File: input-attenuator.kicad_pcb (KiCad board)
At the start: 2 copper layers, 90.2 x 55.8 mm, 100 parts, among them J1 DC_INTF, J2 DC_INTF, J3 RX, J4 ANT, J5 TX, K1 EE2-5TNU-L, K2 EE2-5TNU-L, K3 EE2-5TNU-L, K4 EE2-5TNU-L, Q1 BC858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

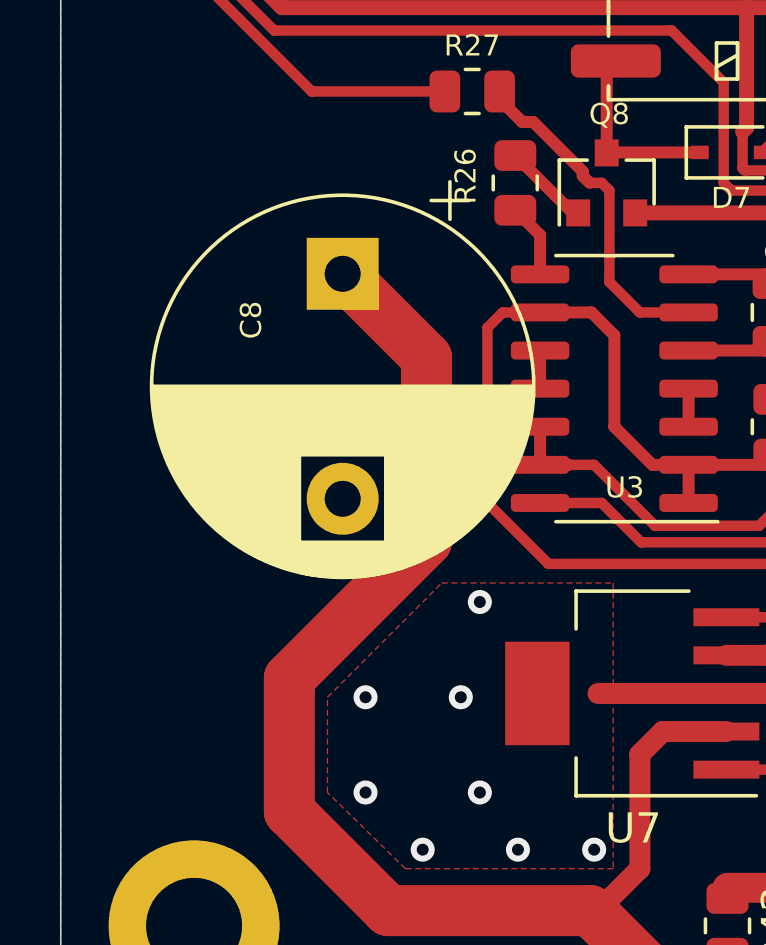
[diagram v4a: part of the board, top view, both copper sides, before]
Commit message: Layout: rotated C8
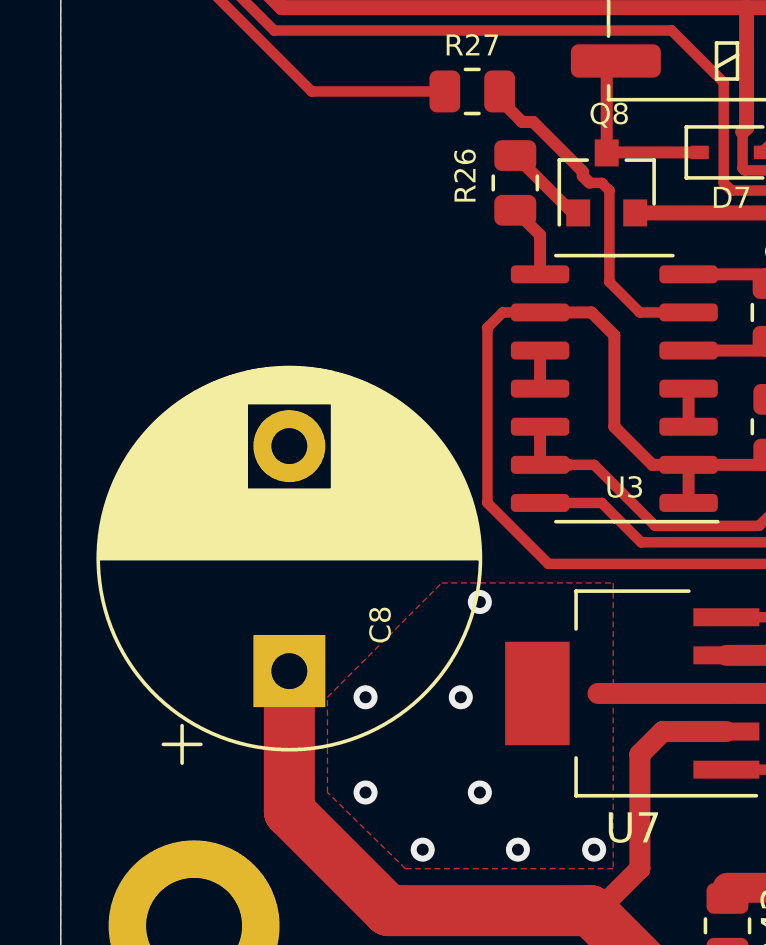
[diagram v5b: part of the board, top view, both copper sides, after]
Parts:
- moved C8 13.4 mm to (71.1, 68.3), turned to 90 degrees
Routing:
- net /Vin2: track 140.4 -> 123.9 mm
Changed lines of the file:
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@@
   )
   (footprint "Capacitor_THT:CP_Radial_D12.5mm_P7.50mm" (layer "F.Cu")
-    (at 72.898 55.100041 -90)
+    (at 71.12 68.343959 90)
     (descr "CP, Radial series, Radial, pin pitch=7.50mm, , diameter=12.5mm, Electrolytic Capacitor")
     (tags "CP Radial series Radial pin pitch 7.50mm  diameter 12.5mm Electrolytic Capacitor")
@@
     (fp_line (start -1.616489 -2.7375) (end -0.366489 -2.7375) (layer "F.Fab") (width 0.1))
     (fp_circle (center 3.75 0) (end 10 0) (layer "F.Fab") (width 0.1) (fill none))
-    (pad "1" thru_hole rect (at 0 0 270) (locked) (size 2.4 2.4) (drill 1.2) (layers *.Cu *.Mask)
+    (pad "1" thru_hole rect (at 0 0 90) (locked) (size 2.4 2.4) (drill 1.2) (layers *.Cu *.Mask)
       (net 4 "/Vin2") (pintype "passive"))
-    (pad "2" thru_hole circle (at 7.5 0 270) (locked) (size 2.4 2.4) (drill 1.2) (layers *.Cu *.Mask)
+    (pad "2" thru_hole circle (at 7.5 0 90) (locked) (size 2.4 2.4) (drill 1.2) (layers *.Cu *.Mask)
       (net 11 "GND") (pintype "passive"))
     (model "${KISYS3DMOD}/Capacitor_THT.3dshapes/CP_Radial_D12.5mm_P7.50mm.wrl"
@@
   (segment (start 71.12 73.025) (end 74.422 76.327) (width 1.7) (layer "F.Cu") (net 4))
   (segment (start 138.377011 72.188989) (end 137.922 72.644) (width 0.35) (layer "F.Cu") (net 4))
-  (segment (start 72.898 55.100041) (end 75.692 57.894041) (width 1.7) (layer "F.Cu") (net 4))
   (segment (start 128.016 76.454) (end 124.587 73.025) (width 0.35) (layer "F.Cu") (net 4))
   (segment (start 83.566 70.358) (end 82.804 71.12) (width 0.7) (layer "F.Cu") (net 4))
   (segment (start 141.171011 72.188989) (end 141.171011 75.490989) (width 0.35) (layer "F.Cu") (net 4))
   (segment (start 143.459489 72.188989) (end 141.171011 72.188989) (width 0.35) (layer "F.Cu") (net 4))
-  (segment (start 75.692 57.894041) (end 75.692 64.008) (width 1.7) (layer "F.Cu") (net 4))
   (segment (start 144.272 73.0015) (end 143.459489 72.188989) (width 0.35) (layer "F.Cu") (net 4))
   (segment (start 128.778 66.294) (end 127.117011 67.954989) (width 1.7) (layer "F.Cu") (net 4))
@@
   (segment (start 83.566 78.74) (end 81.153 76.327) (width 1.7) (layer "F.Cu") (net 4))
   (segment (start 127.117011 67.954989) (end 127.117011 70.494989) (width 1.7) (layer "F.Cu") (net 4))
-  (segment (start 75.692 64.008) (end 71.12 68.58) (width 1.7) (layer "F.Cu") (net 4))
   (segment (start 135.382 62.501959) (end 137.558959 60.325) (width 0.7) (layer "F.Cu") (net 4))
   (segment (start 137.922 72.644) (end 137.922 73.0015) (width 0.35) (layer "F.Cu") (net 4))

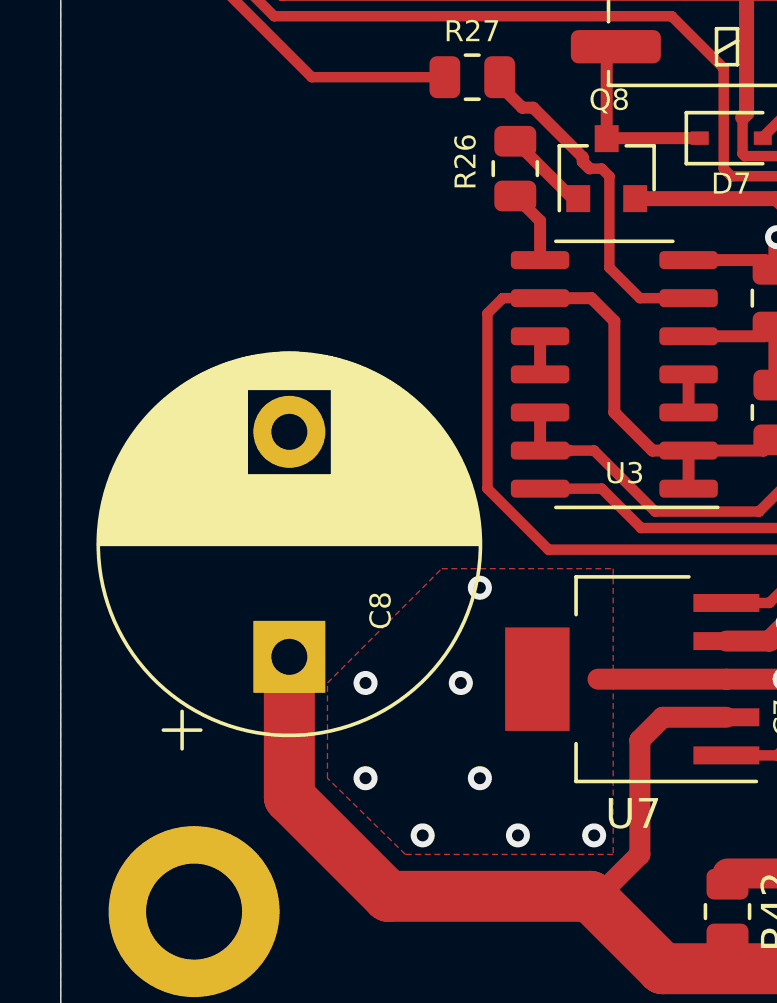
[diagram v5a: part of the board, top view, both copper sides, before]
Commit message: Layout: moved C8 back into position
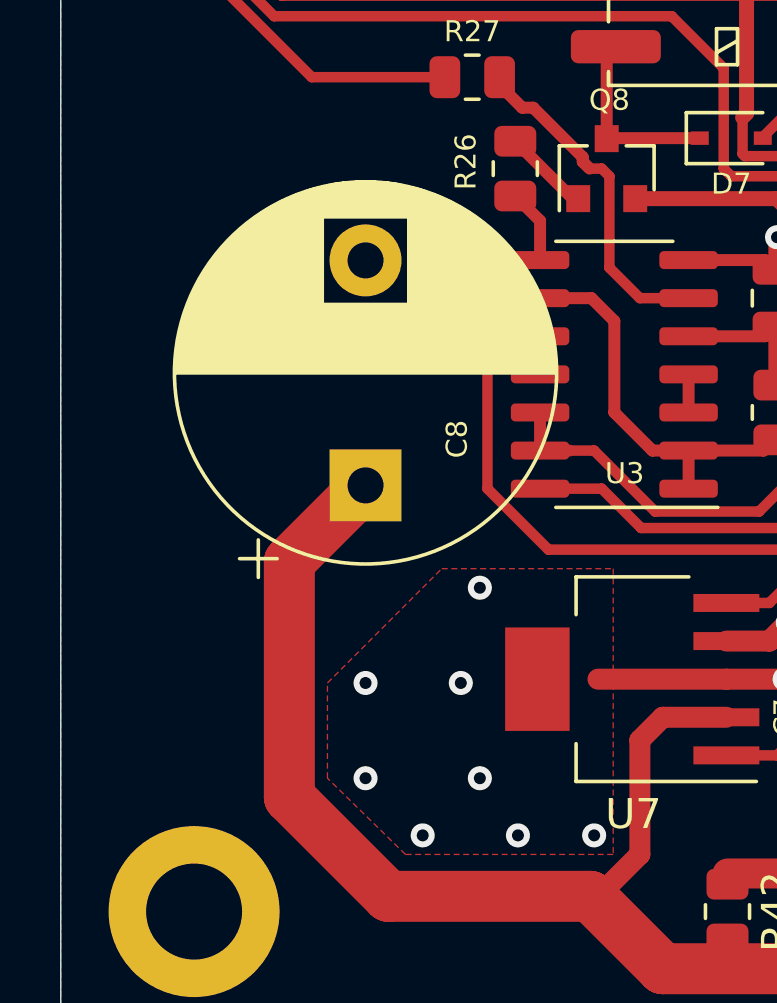
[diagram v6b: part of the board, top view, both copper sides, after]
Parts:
- moved C8 6.25 mm to (73.7, 62.6)
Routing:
- net /Vin2: track 123.9 -> 130.9 mm
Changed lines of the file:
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@@
   )
   (footprint "Capacitor_THT:CP_Radial_D12.5mm_P7.50mm" (layer "F.Cu")
-    (at 71.12 68.343959 90)
+    (at 73.66 62.628959 90)
     (descr "CP, Radial series, Radial, pin pitch=7.50mm, , diameter=12.5mm, Electrolytic Capacitor")
     (tags "CP Radial series Radial pin pitch 7.50mm  diameter 12.5mm Electrolytic Capacitor")
@@
   (segment (start 71.12 73.025) (end 74.422 76.327) (width 1.7) (layer "F.Cu") (net 4))
   (segment (start 138.377011 72.188989) (end 137.922 72.644) (width 0.35) (layer "F.Cu") (net 4))
+  (segment (start 71.12 65.168959) (end 71.12 73.025) (width 1.7) (layer "F.Cu") (net 4))
   (segment (start 128.016 76.454) (end 124.587 73.025) (width 0.35) (layer "F.Cu") (net 4))
   (segment (start 83.566 70.358) (end 82.804 71.12) (width 0.7) (layer "F.Cu") (net 4))
@@
   (segment (start 118.872 78.74) (end 83.566 78.74) (width 1.7) (layer "F.Cu") (net 4))
   (segment (start 131.318 66.294) (end 128.778 66.294) (width 1.7) (layer "F.Cu") (net 4))
-  (segment (start 74.422 76.327) (end 81.153 76.327) (width 1.7) (layer "F.Cu") (net 4))
   (segment (start 140.208 76.454) (end 128.016 76.454) (width 0.35) (layer "F.Cu") (net 4))
-  (segment (start 71.12 68.58) (end 71.12 73.025) (width 1.7) (layer "F.Cu") (net 4))
+  (segment (start 73.66 62.628959) (end 71.12 65.168959) (width 1.7) (layer "F.Cu") (net 4))
   (segment (start 85.6875 70.358) (end 83.566 70.358) (width 0.7) (layer "F.Cu") (net 4))
   (segment (start 81.407 76.327) (end 81.153 76.327) (width 0.25) (layer "F.Cu") (net 4))
   (segment (start 141.171011 75.490989) (end 140.208 76.454) (width 0.35) (layer "F.Cu") (net 4))
+  (segment (start 74.422 76.327) (end 81.153 76.327) (width 1.7) (layer "F.Cu") (net 4))
   (segment (start 83.566 78.74) (end 81.153 76.327) (width 1.7) (layer "F.Cu") (net 4))
   (segment (start 127.117011 67.954989) (end 127.117011 70.494989) (width 1.7) (layer "F.Cu") (net 4))

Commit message: questionsForYou
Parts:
- removed U5: 74HC00, Package_SO:SO-14_3.9x8.65mm_P1.27mm
- added R52: 100k, Resistor_SMD:R_0805_2012Metric, F.Cu at (113.1, 66.3)
- added R53: 100k, Resistor_SMD:R_0805_2012Metric, F.Cu at (111.3, 66.3)
- added R54: 100k, Resistor_SMD:R_0805_2012Metric, F.Cu at (110.8, 59.5)
- added R55: 100k, Resistor_SMD:R_0805_2012Metric, F.Cu at (87.1, 50.8)
- added R56: 100k, Resistor_SMD:R_0805_2012Metric, F.Cu at (73.7, 58.6)
- added R59: 1M, Resistor_SMD:R_0805_2012Metric, F.Cu at (150.3, 63.3)
- R33: value 1M -> 100k
- U6: value 74HC595 -> MCP23017_SO; footprint Package_SO:SO-16_3.9x9.9mm_P1.27mm -> Package_SO:SOIC-28W_7.5x17.9mm_P1.27mm
- moved R33 23.6 mm to (110.5, 63.2), turned to -90 degrees
- moved C2 8.18 mm to (98.6, 70.2), turned to 0 degrees
- moved U6 6.28 mm to (103.0, 59.8)
- moved R27 3.77 mm to (73.5, 49.3), turned to 90 degrees
- moved R25 2.85 mm to (87.1, 52.9)
- moved C6 2.77 mm to (84.5, 56.3)
- moved D7 2.77 mm to (83.1, 51.0)
- moved D9 2.77 mm to (90.4, 72.8)
- moved R24 2.77 mm to (90.4, 52.0)
- moved R30 2.77 mm to (84.5, 60.1)
- moved C5 2.77 mm to (95.3, 56.3)
- moved C7 2.77 mm to (86.4, 70.1)
- moved C8 2.77 mm to (70.9, 62.6)
- moved D10 2.77 mm to (94.5, 68.5)
- moved Q6 2.77 mm to (93.9, 52.0)
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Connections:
- C2 pad 1: GND -> +5V
- C2 pad 2: +5V -> GND
- J1 pad 3: Net-(J1-Pad3) -> /SDA
- J1 pad 4: Net-(J1-Pad4) -> /SCL
- J1 pad 5: Net-(J1-Pad5) -> unconnected-(J1-Pad5)
- J1 pad 6: Net-(J1-Pad6) -> /SCL
- J2 pad 3: Net-(J1-Pad3) -> /SDA
- J2 pad 4: Net-(J1-Pad4) -> /SCL
- J2 pad 5: Net-(J1-Pad6) -> /SCL
- R1 pad 1: Net-(R1-Pad1) -> Net-(U1-Pad6)
- R2 pad 1: Net-(R2-Pad1) -> Net-(U1-Pad8)
- R22 pad 1: Net-(R22-Pad1) -> Net-(U4-Pad6)
- R26 pad 1: Net-(R26-Pad1) -> Net-(U3-Pad6)
- R27 pad 1: Net-(R27-Pad1) -> Net-(U3-Pad8)
- R28 pad 1: Net-(R28-Pad1) -> Rx
- R29 pad 1: Net-(R29-Pad1) -> 10dB
- R3 pad 1: Net-(R3-Pad1) -> 5dB
- R30 pad 1: Net-(R30-Pad1) -> 20dB
- R33 pad 1: /PowerDn -> Rx
- R33 pad 2: /Vin2 -> GND
- U1 pad 1: Net-(R3-Pad1) -> 5dB
- U1 pad 2: Net-(R3-Pad1) -> 5dB
- U1 pad 6: Net-(R2-Pad1) -> Net-(U1-Pad6)
- U1 pad 8: Net-(R1-Pad1) -> Net-(U1-Pad8)
- U1 pad 9: Net-(R3-Pad1) -> 5dB
- U2 pad 1: Net-(R29-Pad1) -> 10dB
- U2 pad 2: Net-(R29-Pad1) -> 10dB
- U2 pad 6: Net-(R25-Pad1) -> Net-(R24-Pad1)
- U2 pad 8: Net-(R24-Pad1) -> Net-(R25-Pad1)
- U2 pad 9: Net-(R29-Pad1) -> 10dB
- U3 pad 1: Net-(R30-Pad1) -> 20dB
- U3 pad 2: Net-(R30-Pad1) -> 20dB
- U3 pad 6: Net-(R27-Pad1) -> Net-(U3-Pad6)
- U3 pad 8: Net-(R26-Pad1) -> Net-(U3-Pad8)
- U3 pad 9: Net-(R30-Pad1) -> 20dB
- U4 pad 1: Net-(R28-Pad1) -> Rx
- U4 pad 2: Net-(R28-Pad1) -> Rx
- U4 pad 6: Net-(R23-Pad1) -> Net-(U4-Pad6)
- U4 pad 8: Net-(R22-Pad1) -> Net-(R23-Pad1)
- U4 pad 9: Net-(R28-Pad1) -> Rx
- U6 pad 1: 20dB -> unconnected-(U6-Pad1)
- U6 pad 10: +5V -> GND
- U6 pad 11: Net-(J1-Pad5) -> unconnected-(U6-Pad11)
- U6 pad 12: Net-(J1-Pad4) -> /SCL
- U6 pad 13: GND -> /SDA
- U6 pad 14: Net-(J1-Pad3) -> unconnected-(U6-Pad14)
- U6 pad 15: Rx -> +5V
- U6 pad 16: +5V -> GND
- U6 pad 2: 10dB -> unconnected-(U6-Pad2)
- U6 pad 3: 5dB -> unconnected-(U6-Pad3)
- U6 pad 7: unconnected-(U6-Pad7) -> 10dB
- U6 pad 8: GND -> 20dB
- U6 pad 9: Net-(J1-Pad6) -> +5V
- U8 pad 1: (no net) -> /IIC_Reset
- U8 pad 6: (no net) -> Net-(R31-Pad2)
- U8 pad 7: (no net) -> +5V
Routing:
- net /SCL: track 0.00 -> 88.0 mm, vias 0 -> 1
- net Net-(R30-Pad1): track 52.8 -> 0.00 mm
- net 20dB: track 5.32 -> 48.5 mm
- net Net-(R28-Pad1): track 43.1 -> 0.00 mm
- net Net-(J1-Pad6): track 41.9 -> 0.00 mm, vias 1 -> 0
- net Net-(J1-Pad4): track 40.0 -> 0.00 mm, vias 1 -> 0
- net Net-(J1-Pad3): track 37.5 -> 0.00 mm, vias 1 -> 0
- net Rx: track 6.94 -> 39.2 mm
- net /PowerDn: track 105.4 -> 73.2 mm, vias 2 -> 0
- net Net-(R3-Pad1): track 26.9 -> 0.00 mm
- net Net-(R29-Pad1): track 24.5 -> 0.00 mm
- net /Vin: track 47.0 -> 70.8 mm
- net Net-(J1-Pad5): track 19.2 -> 0.00 mm, vias 1 -> 0
- net GND: track 167.2 -> 150.7 mm, vias 25 -> 29
- net unconnected-(J1-Pad5): track 0.00 -> 15.9 mm, vias 0 -> 1
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
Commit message: final
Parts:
- removed J2: DC_INTF, Connector_PinHeader_2.54mm:PinHeader_1x07_P2.54mm_Vertical
- removed R59: 1M, Resistor_SMD:R_0805_2012Metric
- moved R44 38.3 mm to (142.4, 70.0), turned to 90 degrees
- moved R50 32.6 mm to (130.9, 74.0)
- moved R46 32.3 mm to (133.8, 73.9)
- moved R45 29.0 mm to (136.8, 73.9)
- moved R51 28.8 mm to (139.8, 73.9)
- moved R47 28.2 mm to (142.4, 73.9)
- moved R48 11.7 mm to (83.7, 74.5)
- moved Q10 10.9 mm to (125.3, 67.8)
- moved Q3 10.9 mm to (132.2, 67.8)
- moved R36 10.9 mm to (135.2, 67.8), turned to -90 degrees
- moved R39 10.9 mm to (128.9, 67.8)
- moved R41 10.9 mm to (122.0, 67.8)
- moved R40 10.5 mm to (119.9, 67.9), turned to -90 degrees
- moved R32 9.26 mm to (131.0, 71.1)
- moved D9 6.82 mm to (94.9, 67.7)
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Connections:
- J1 pad 5: unconnected-(J1-Pad5) -> /SHDN
- J1 pad 6: /SCL -> unconnected-(J1-Pad6)
- J1 pad 7: /SHDN -> unconnected-(J1-Pad7)
- Q3 pad 3: /PowerDn -> /IIC_Reset
- R31 pad 1: /PowerDn -> /IIC_Reset
- R36 pad 1: /PowerDn -> /IIC_Reset
- U8 pad 1: /IIC_Reset -> (no net)
- U8 pad 2: /PowerDn -> /IIC_Reset
- U8 pad 6: Net-(R31-Pad2) -> (no net)
- U8 pad 7: +5V -> (no net)
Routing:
- net /PowerDn: track 73.2 -> 0.00 mm
- net /SCL: track 88.0 -> 22.3 mm, vias 1 -> 0
- net /IIC_Reset: track 0.00 -> 45.6 mm
- net /Vin: track 70.8 -> 29.6 mm, vias 4 -> 0
- net +5V: track 221.6 -> 261.9 mm, vias 6 -> 8
- net Net-(D10-Pad1): track 39.4 -> 63.1 mm
- net /Vin2: track 146.1 -> 129.3 mm, vias 2 -> 0
- net /SHDN: track 46.6 -> 29.9 mm, vias 1 -> 0
- net unconnected-(J1-Pad5): track 15.9 -> 0.00 mm, vias 1 -> 0
- net Net-(R31-Pad2): track 19.9 -> 31.5 mm, vias 0 -> 2
- net Net-(U1-Pad6): track 0.00 -> 10.2 mm, vias 0 -> 2
- net /SDA: track 8.69 -> 18.6 mm
- net Net-(U4-Pad6): track 0.40 -> 9.89 mm, vias 0 -> 2
- net Net-(C6-Pad1): track 20.6 -> 13.5 mm, vias 0 -> 2
- net Net-(Q7-Pad1): track 42.9 -> 39.1 mm
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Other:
- board size 90.2 x 55.8 mm -> 90.1 x 52.5 mm
- board text added: "Input Attenuator v1.5 26.07.2021"
- board text removed: "Input Attenuator v1.4 22.03.2021"
